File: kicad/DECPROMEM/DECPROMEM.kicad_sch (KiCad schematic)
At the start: 136 parts, among them J10 BDAL08, J100 A15, J101 A16, J102 A17, J103 A18, J104 A19, J105 A20, J106 A21, J107 +5V, J11 BDAL09, J12 BDAL10, J13 BDAL11, J14 BDAL12, J15 BDAL13, J16 BDAL14, J17 BDAL15, J18 BDAL16, J19 BDAL17, J2 BDAL00, J20 BDAL18, J21 BDAL19, J22 BDAL20, J23 BDAL21, J24 BRPLYL, J25 BMDENL, J26 BWRITEL, J27 BWLBL, J28 BWHBL, J29 BSDENL, J3 BDAL01, J30 SSnL, J31 BDSL, J32 BASL, J33 BIOSELL, J34 BDCOKH, J35 GND, J36 GND, J37 GND, J38 DAH00, J39 DAH01, J4 BDAL02, J40 DAH02, J41 DAH03, J42 DAH04, J43 DAH05, J44 DAH06, J45 DAH07, J46 DAH08, J47 DAH09, J48 DAH10, J49 DAH11, J5 BDAL03, J50 DAH12, J51 DAH13, J52 DAH14, J53 DAH15, J54 DAH16, J55 DAH17, J56 DAH18, J57 DAH19, J58 DAH20, J59 DAH21, J6 BDAL04, J60 JTAG, J61 ASL, J62 MDENL, J63 SDENL, J64 MOEL, J65 MWEL, J66 MCELOWH, J67 MLEL, J68 MCEHIGHL, J69 MHEL, J7 BDAL05, J70 BUSDIR, J71 BUSOE, J72 CLK, J73 MA15, J74 MA16, J75 MA17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

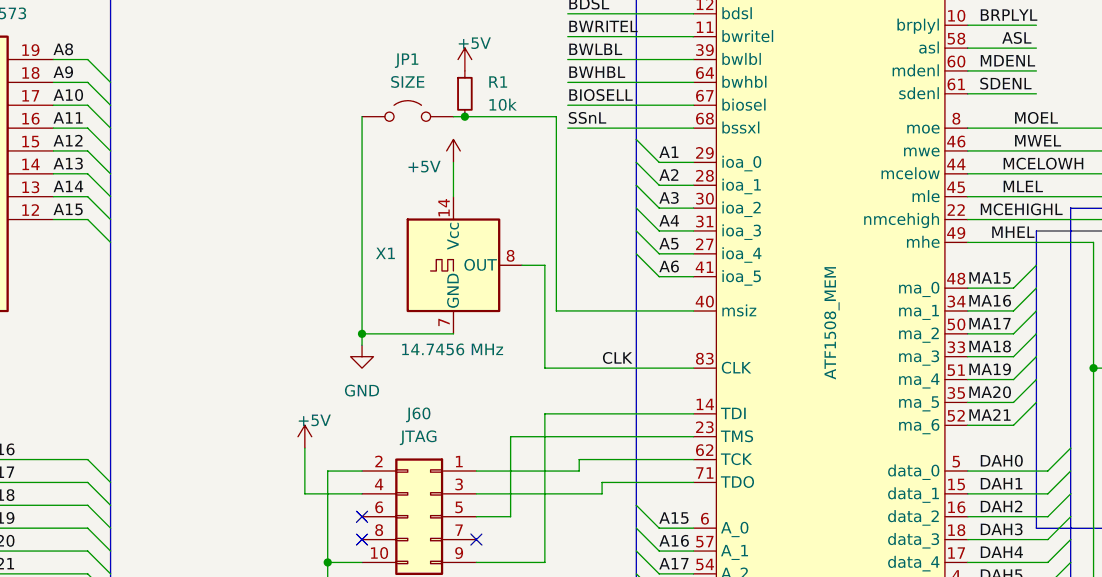
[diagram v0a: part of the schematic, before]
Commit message: Updating pinout for large connector since it was wrong. Added support for 245 trancerivers.
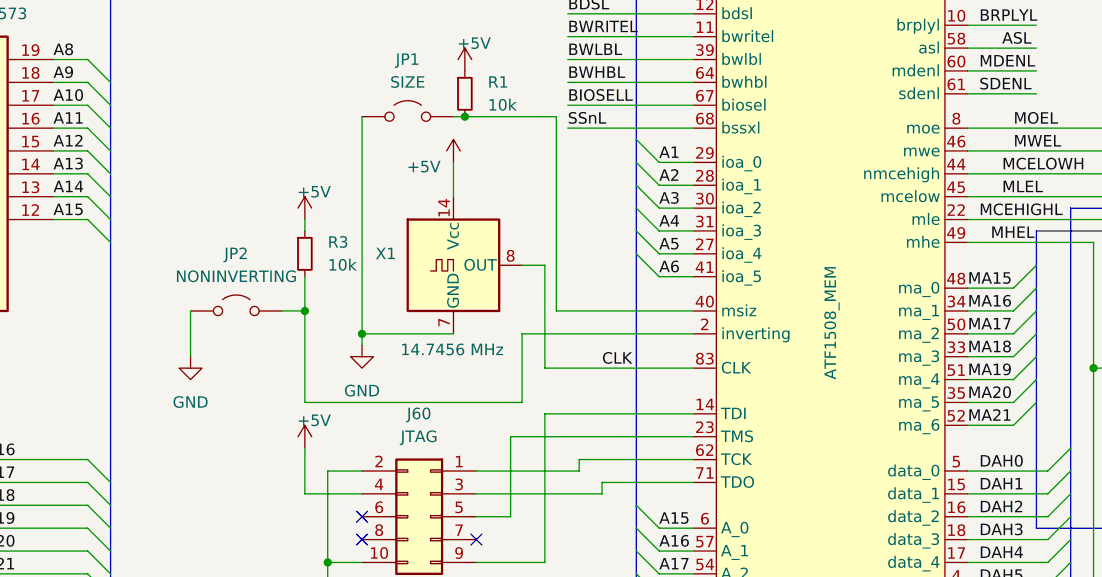
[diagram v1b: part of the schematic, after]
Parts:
- added JP2: NONINVERTING, Connector_PinHeader_2.54mm:PinHeader_1x02_P2.54mm_Vertical, symbol Jumper:Jumper_2_Open
- added R3: 10k, Resistor_THT:R_Axial_DIN0207_L6.3mm_D2.5mm_P10.16mm_Horizontal, symbol Device:R_Small
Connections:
- net +5V: now also R3.1
- net GND: now also JP2.1 (A)
- new net: JP2.2 (B), R3.2, U11.2 (inverting)
